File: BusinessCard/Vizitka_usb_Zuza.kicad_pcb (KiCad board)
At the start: 2 copper layers, 90 x 50 mm, 88 parts, among them J1 AVR-ISP-6, J2 USB_C_Receptacle, J3 Conn_01x01, Q1 MMBT3904, Q11 MMBT3904, Q3 MMBT3904, Q5 MMBT3904, U1 ATmega328P-AU, U2 DS18B20, U4 DS18B20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

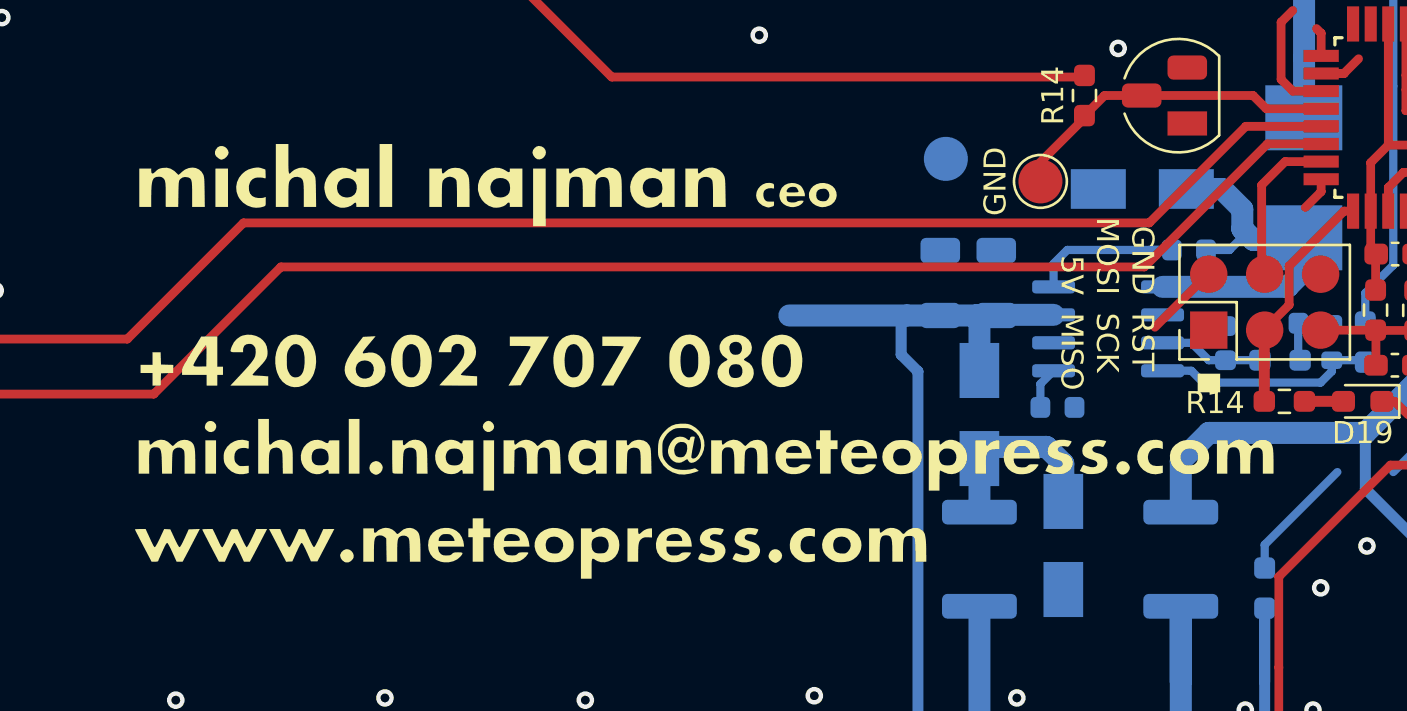
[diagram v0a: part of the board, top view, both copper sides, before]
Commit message: Added aditional businesscards - Zuza, MichalModra...Actual Tapeout 2023-08-24, but repaired connection!
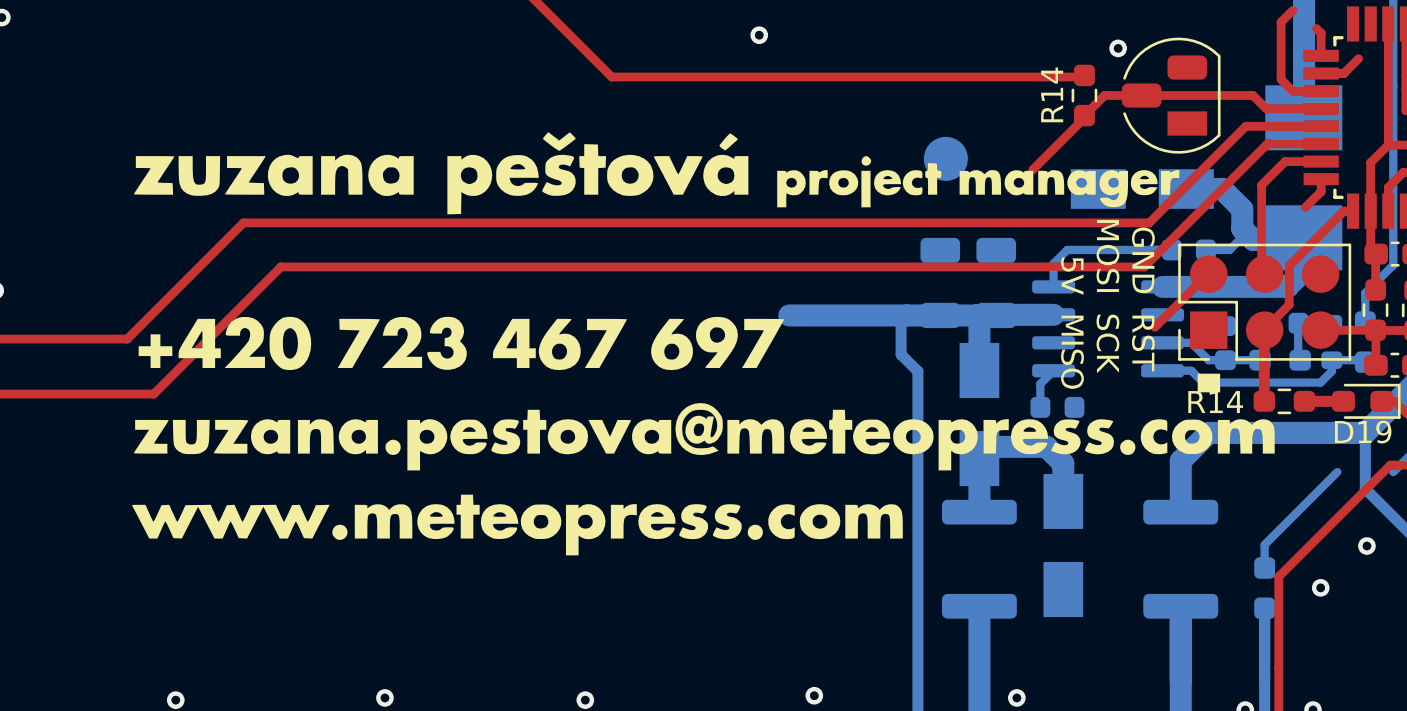
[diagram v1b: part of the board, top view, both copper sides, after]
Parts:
- removed TP18: GND, meteopress:TestPoint_THTPad_D2.0mm_Drill1.0mm
- G***: footprint meteopress:MichalNajman -> meteopress:ZuzanaPestova
- G***: footprint meteopress:vCard_MichalNajman_30 -> meteopress:vCard_ZuzanaPestova_30
- moved G*** 0.80 mm to (134.0, 132.2)
